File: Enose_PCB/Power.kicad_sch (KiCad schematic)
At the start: 53 parts, among them IC1 ISL91127IRNZ-T7A, J5 USB_C_Receptacle_USB2.0_16P, J6 Battery Terminal, SW3 SW_DPST_x2, U2 USBLC6-2P6, U3 MP2721GRH-0000-P

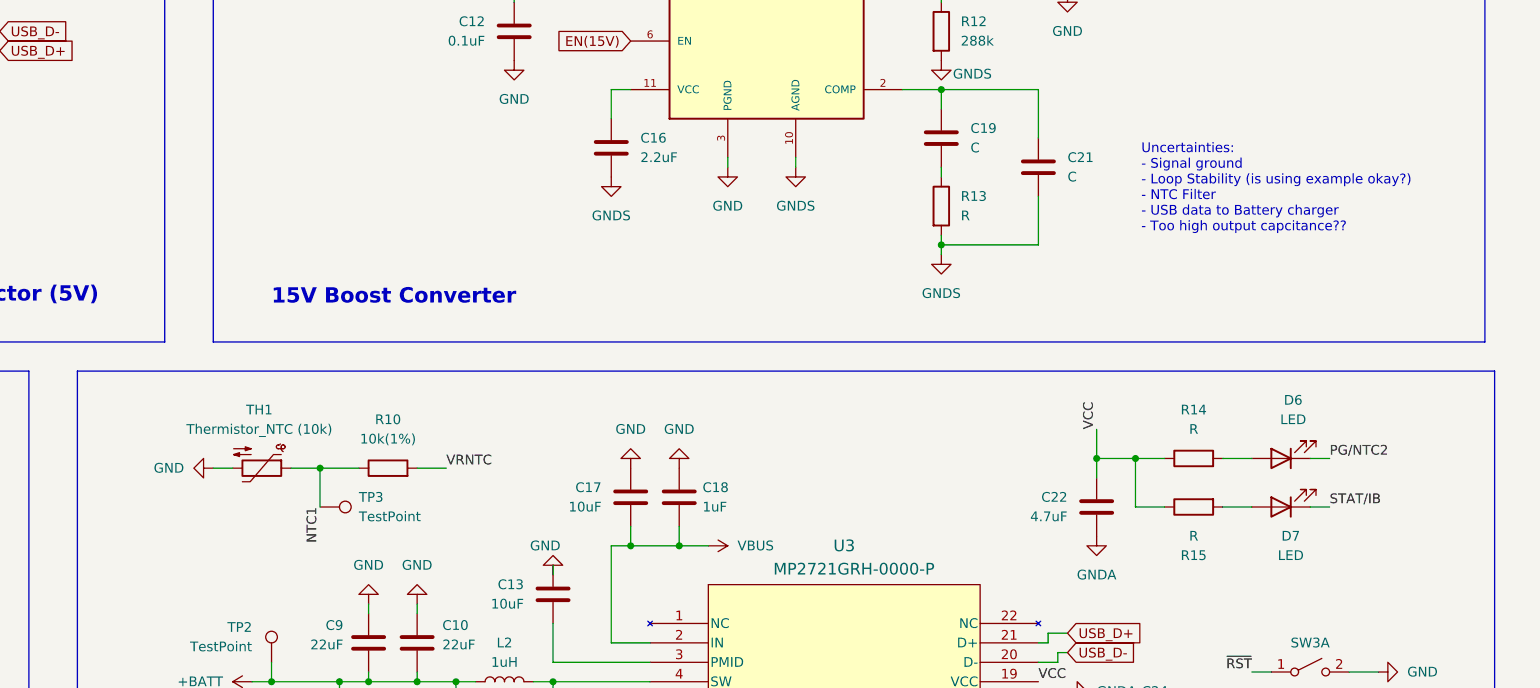
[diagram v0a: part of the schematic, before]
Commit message: Updated component values
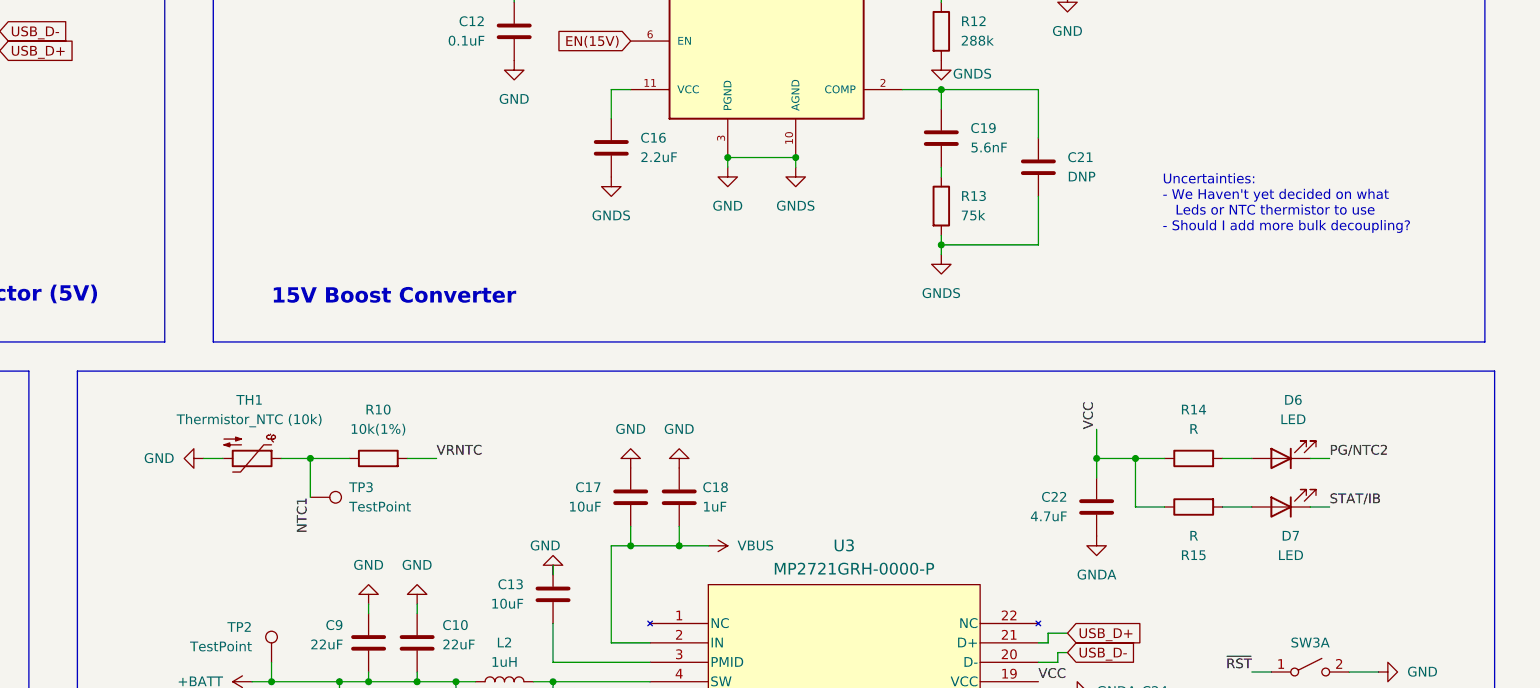
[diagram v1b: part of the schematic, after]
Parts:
- C19: value C -> 5.6nF
- C21: value C -> DNP
- R13: value R -> 75k
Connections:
- net GNDS is gone; now on net GND: C16.2, C21.2, PS1.10 (AGND), R12.2, R13.2
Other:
- note added: "Uncertainties: - We Haven't yet decided on what Leds or NTC thermistor to use - Should I add more bulk decoupling?"
- note removed: "Uncertainties: - Signal ground - Loop Stability (is using example okay?) - NTC Filter - USB data to Battery charger - Too high output capcitance??"
- moved on the sheet: R10, TH1, TP3
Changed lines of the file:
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@@
 		)
 	)
-	(text "Uncertainties:\n- Signal ground\n- Loop Stability (is using example okay?)\n- NTC Filter\n- USB data to Battery charger\n- Too high output capcitance??\n"
+	(text "Uncertainties:\n- We Haven't yet decided on what \n   Leds or NTC thermistor to use\n- Should I add more bulk decoupling?\n"
 		(exclude_from_sim no)
-		(at 235.712 65.024 0)
+		(at 238.506 67.056 0)
 		(effects
 			(font
@@
 	)
 	(junction
+		(at 190.5 60.96)
+		(diameter 0)
+		(color 0 0 0 0)
+	)
+	(junction
 		(at 72.39 135.89)
 		(diameter 0)
@@
 	)
 	(junction
-		(at 128.27 101.6)
+		(at 127 100.33)
 		(diameter 0)
 		(color 0 0 0 0)
@@
 	)
 	(junction
+		(at 181.61 60.96)
+		(diameter 0)
+		(color 0 0 0 0)
+	)
+	(junction
 		(at 234.95 100.33)
 		(diameter 0)
@@
 	(wire
 		(pts
-			(xy 124.46 101.6) (xy 128.27 101.6)
+			(xy 123.19 100.33) (xy 127 100.33)
 		)
 		(stroke
@@
 	(wire
 		(pts
+			(xy 181.61 60.96) (xy 190.5 60.96)
+		)
+		(stroke
+			(width 0)
+			(type default)
+		)
+	)
+	(wire
+		(pts
 			(xy 153.67 39.37) (xy 153.67 40.64)
 		)
@@
 	(wire
 		(pts
-			(xy 133.35 101.6) (xy 128.27 101.6)
+			(xy 132.08 100.33) (xy 127 100.33)
 		)
 		(stroke
@@
 	(wire
 		(pts
-			(xy 128.27 101.6) (xy 128.27 106.68)
+			(xy 127 100.33) (xy 127 105.41)
 		)
 		(stroke
@@
 	(wire
 		(pts
-			(xy 114.3 101.6) (xy 116.84 101.6)
+			(xy 113.03 100.33) (xy 115.57 100.33)
 		)
 		(stroke
@@
 	(wire
 		(pts
-			(xy 140.97 101.6) (xy 144.78 101.6)
+			(xy 139.7 100.33) (xy 143.51 100.33)
 		)
 		(stroke
@@
 	)
 	(label "NTC1"
-		(at 128.27 106.68 270)
+		(at 127 105.41 270)
 		(effects
 			(font
@@
 	)
 	(label "VRNTC"
-		(at 144.78 101.6 0)
+		(at 143.51 100.33 0)
 		(effects
 			(font
@@
 	(symbol
 		(lib_id "Device:R")
-		(at 137.16 101.6 90)
+		(at 135.89 100.33 90)
 		(unit 1)
 		(exclude_from_sim no)
@@
 		(fields_autoplaced yes)
 		(property "Reference" "R10"
-			(at 137.16 95.25 90)
+			(at 135.89 93.98 90)
 			(effects
 				(font
@@
 		)
 		(property "Value" "10k(1%)"
-			(at 137.16 97.79 90)
+			(at 135.89 96.52 90)
 			(effects
 				(font
@@
 		)
 		(property "Footprint" ""
-			(at 137.16 103.378 90)
+			(at 135.89 102.108 90)
 			(effects
 				(font
@@
 		)
 		(property "Datasheet" "~"
-			(at 137.16 101.6 0)
+			(at 135.89 100.33 0)
 			(effects
 				(font
@@
 		)
 		(property "Description" "Resistor"
-			(at 137.16 101.6 0)
+			(at 135.89 100.33 0)
 			(effects
 				(font
@@
 			)
 		)
-		(property "Value" "R"
+		(property "Value" "75k"
 			(at 212.09 68.5799 0)
 			(effects
@@
 	(symbol
 		(lib_id "Connector:TestPoint")
-		(at 128.27 106.68 270)
+		(at 127 105.41 270)
 		(unit 1)
 		(exclude_from_sim no)
@@
 		(fields_autoplaced yes)
 		(property "Reference" "TP3"
-			(at 133.35 105.4099 90)
+			(at 132.08 104.1399 90)
 			(effects
 				(font
@@
 		)
 		(property "Value" "TestPoint"
-			(at 133.35 107.9499 90)
+			(at 132.08 106.6799 90)
 			(effects
 				(font
@@
 		)
 		(property "Footprint" ""
-			(at 128.27 111.76 0)
+			(at 127 110.49 0)
 			(effects
 				(font
@@
 		)
 		(property "Datasheet" "~"
-			(at 128.27 111.76 0)
+			(at 127 110.49 0)
 			(effects
 				(font
@@
 		)
 		(property "Description" "test point"
-			(at 128.27 106.68 0)
+			(at 127 105.41 0)
 			(effects
 				(font
@@
 			)
 		)
-		(property "Value" "C"
+		(property "Value" "5.6nF"
 			(at 213.36 59.6899 0)
 			(effects
@@
 	(symbol
 		(lib_id "Device:Thermistor_NTC")
-		(at 120.65 101.6 270)
+		(at 119.38 100.33 270)
 		(unit 1)
 		(exclude_from_sim no)
@@
 		(fields_autoplaced yes)
 		(property "Reference" "TH1"
-			(at 120.3325 93.98 90)
+			(at 119.0625 92.71 90)
 			(effects
 				(font
@@
 		)
 		(property "Value" "Thermistor_NTC (10k)"
-			(at 120.3325 96.52 90)
+			(at 119.0625 95.25 90)
 			(effects
 				(font
@@
 		)
 		(property "Footprint" ""
-			(at 121.92 101.6 0)
+			(at 120.65 100.33 0)
 			(effects
 				(font
@@
 		)
 		(property "Datasheet" "~"
-			(at 121.92 101.6 0)
+			(at 120.65 100.33 0)
 			(effects
 				(font
@@
 		)
 		(property "Description" "Temperature dependent resistor, negative temperature coefficient"
-			(at 120.65 101.6 0)
+			(at 119.38 100.33 0)
 			(effects
 				(font
@@
 	(symbol
 		(lib_id "power:GND")
-		(at 114.3 101.6 270)
+		(at 113.03 100.33 270)
 		(unit 1)
 		(exclude_from_sim no)
@@
 		(fields_autoplaced yes)
 		(property "Reference" "#PWR054"
-			(at 107.95 101.6 0)
+			(at 106.68 100.33 0)
 			(effects
 				(font
@@
 		)
 		(property "Value" "GND"
-			(at 110.49 101.5999 90)
+			(at 109.22 100.3299 90)
 			(effects
 				(font
@@
 		)
 		(property "Footprint" ""
-			(at 114.3 101.6 0)
+			(at 113.03 100.33 0)
 			(effects
 				(font
@@
 		)
 		(property "Datasheet" ""
-			(at 114.3 101.6 0)
+			(at 113.03 100.33 0)
 			(effects
 				(font
@@
 		)
 		(property "Description" "Power symbol creates a global label with name \"GND\" , ground"
-			(at 114.3 101.6 0)
+			(at 113.03 100.33 0)
 			(effects
 				(font
@@
 			)
 		)
-		(property "Value" "C"
+		(property "Value" "DNP"
 			(at 226.06 63.4999 0)
 			(effects
